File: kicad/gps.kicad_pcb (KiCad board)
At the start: 4 copper layers, 84.1 x 61.7 mm, 68 parts, among them J1 Bus_PCI_Express_x1, J2 USB_C_Receptacle_USB2.0_16P, J3 Conn_01x02, J4 USB_C_Receptacle_USB2.0_16P, Q1 IRLML6344, U2 W25Q128JVP, U3 MCP25625T-E/ML, U4 RP2040, U5 NEO-M9N, X1 ABM8-272-T3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

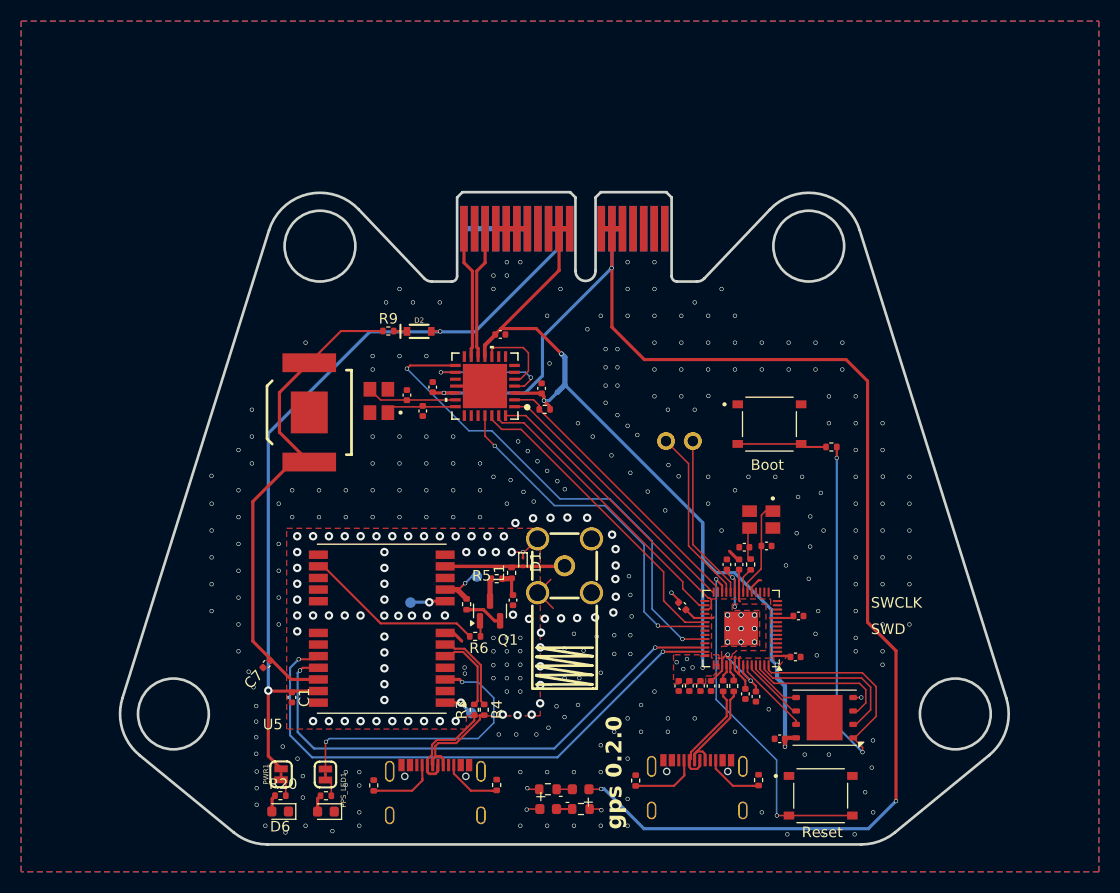
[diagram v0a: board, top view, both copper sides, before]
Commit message: Fix Battery Position
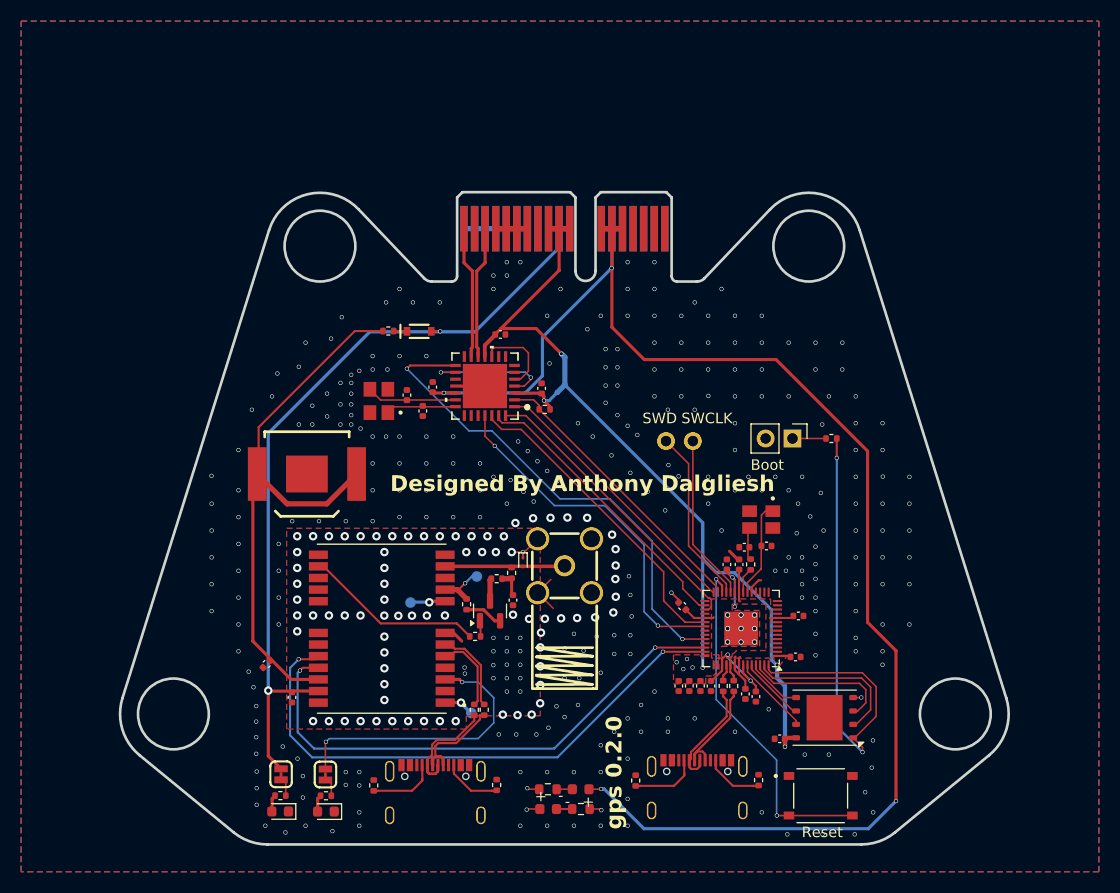
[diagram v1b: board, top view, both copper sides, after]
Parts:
- removed S1: TS-1187A-B-A-B, TS-1187A-B-A-B:SW_TS-1187A-B-A-B
- added J5: Conn_01x02_Pin, Connector_PinHeader_2.54mm:PinHeader_1x02_P2.54mm_Vertical, F.Cu at (168.0, 84.0)
- moved BAT1 5.84 mm to (122.0, 87.4), turned to 0 degrees
- moved R8 0.80 mm to (171.7, 84.0)
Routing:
- net /BACKUP: track 47.8 -> 55.4 mm
- net /~{USB_BOOT_S}: track 8.76 -> 3.18 mm
- net +5V: track 140.9 -> 137.0 mm
- net GND: track 29.0 -> 30.7 mm, vias 357 -> 389
- net /QSPI_SS: track 48.8 -> 49.6 mm
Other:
- board text added: "Designed By Anthony Dalgliesh"

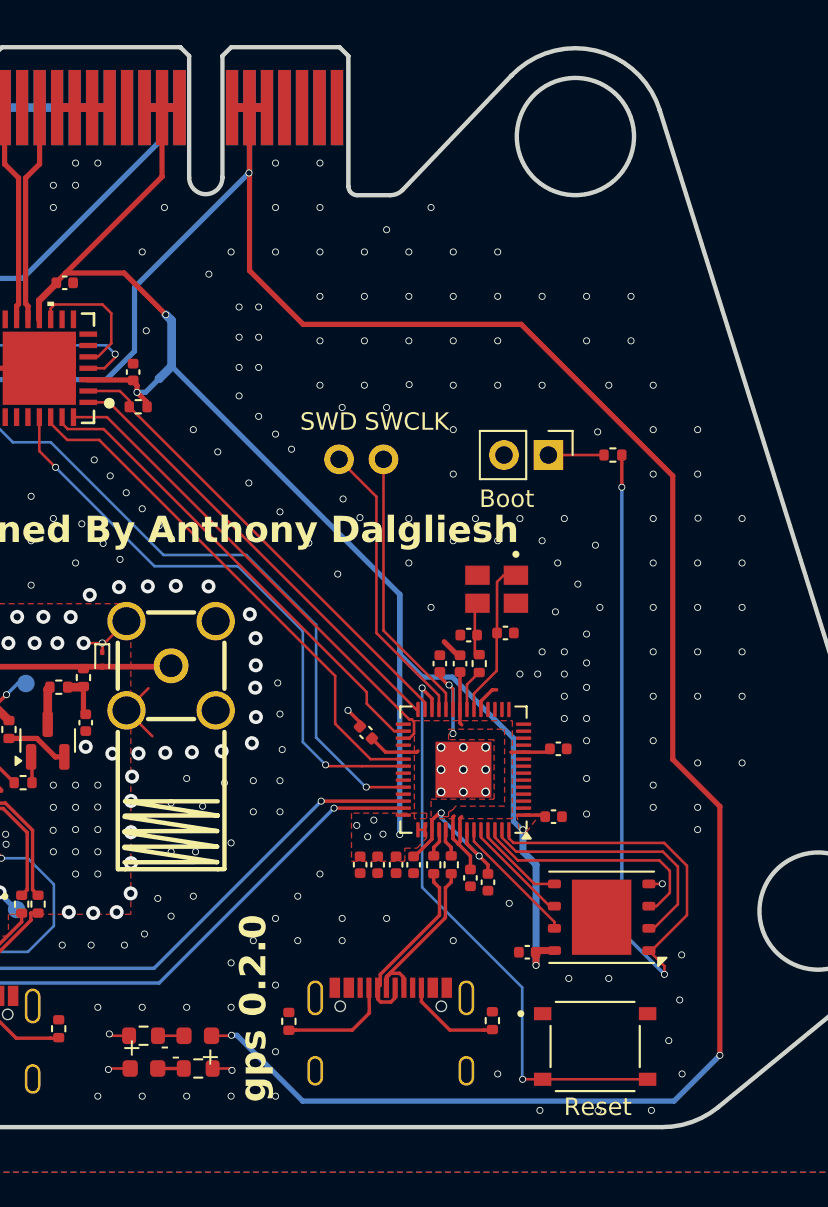
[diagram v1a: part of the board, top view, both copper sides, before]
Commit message: Update components for order
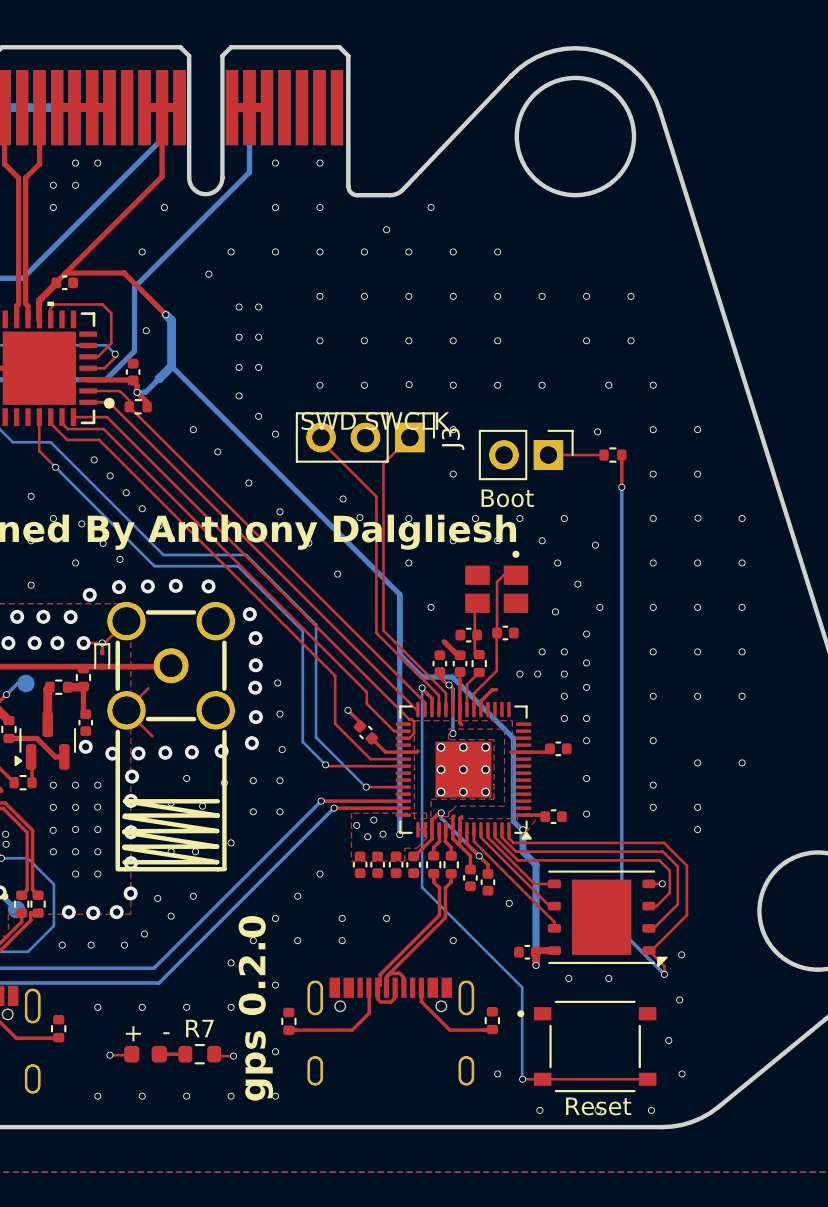
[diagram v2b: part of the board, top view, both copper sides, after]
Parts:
- removed D4: LED, LED_SMD:LED_0603_1608Metric
- removed R10, R13: 1k, Resistor_SMD:R_0603_1608Metric
- added R7: 1 k, Resistor_SMD:R_0603_1608Metric, F.Cu at (148.1, 118.2)
- J3: value Conn_01x02 -> Conn_01x03; footprint Connector_PinHeader_2.54mm:PinHeader_1x02_P2.54mm_Vertical -> Connector_PinHeader_2.54mm:PinHeader_1x03_P2.54mm_Vertical
- moved J3 1.96 mm to (160.1, 83.0)
- moved D3 0.82 mm to (145.0, 118.2)
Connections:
- J3 pad 2: /SWD -> GND
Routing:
- net +5V: track 137.0 -> 32.7 mm, vias 4 -> 1
- net /SWCLK: track 15.8 -> 17.7 mm
- net /SWD: track 16.7 -> 18.3 mm
- net Net-(D4-K): track 1.49 -> 0.00 mm
- net GND: track 30.7 -> 29.5 mm, vias 389 -> 385

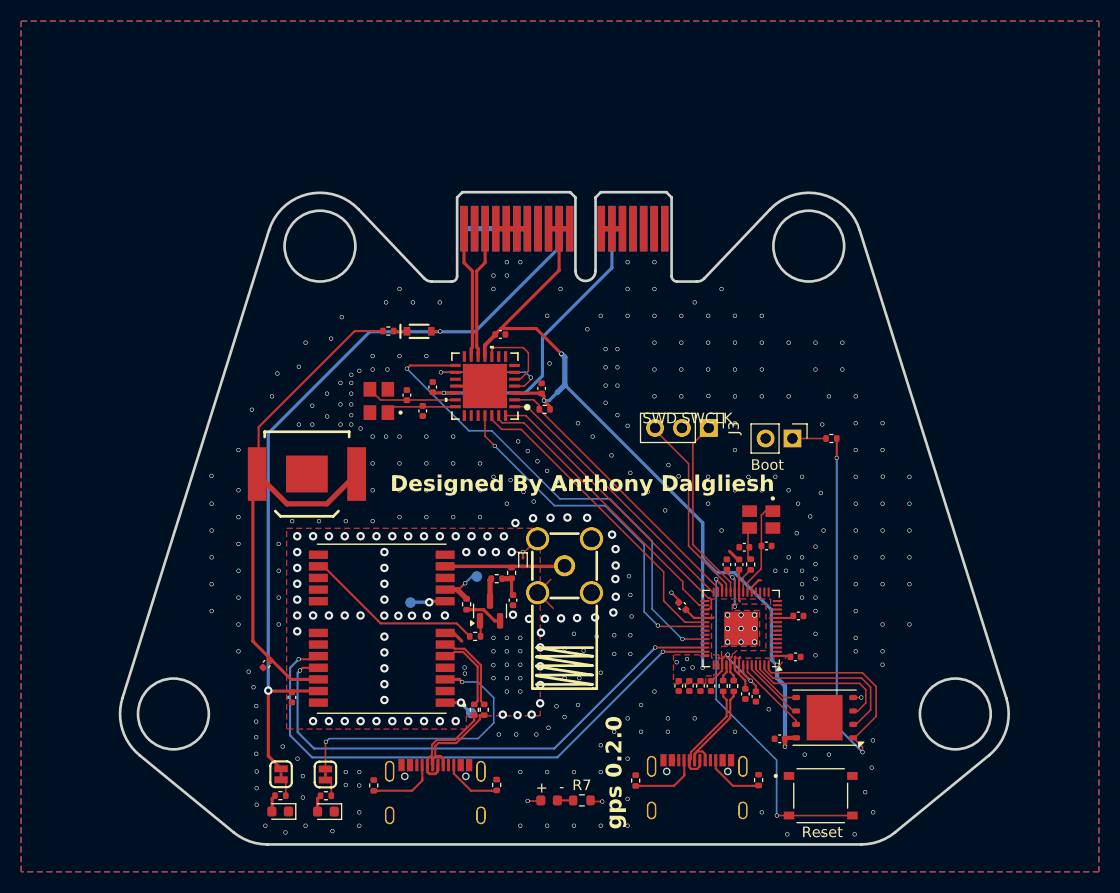
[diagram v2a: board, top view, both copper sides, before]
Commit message: Move Boot pins
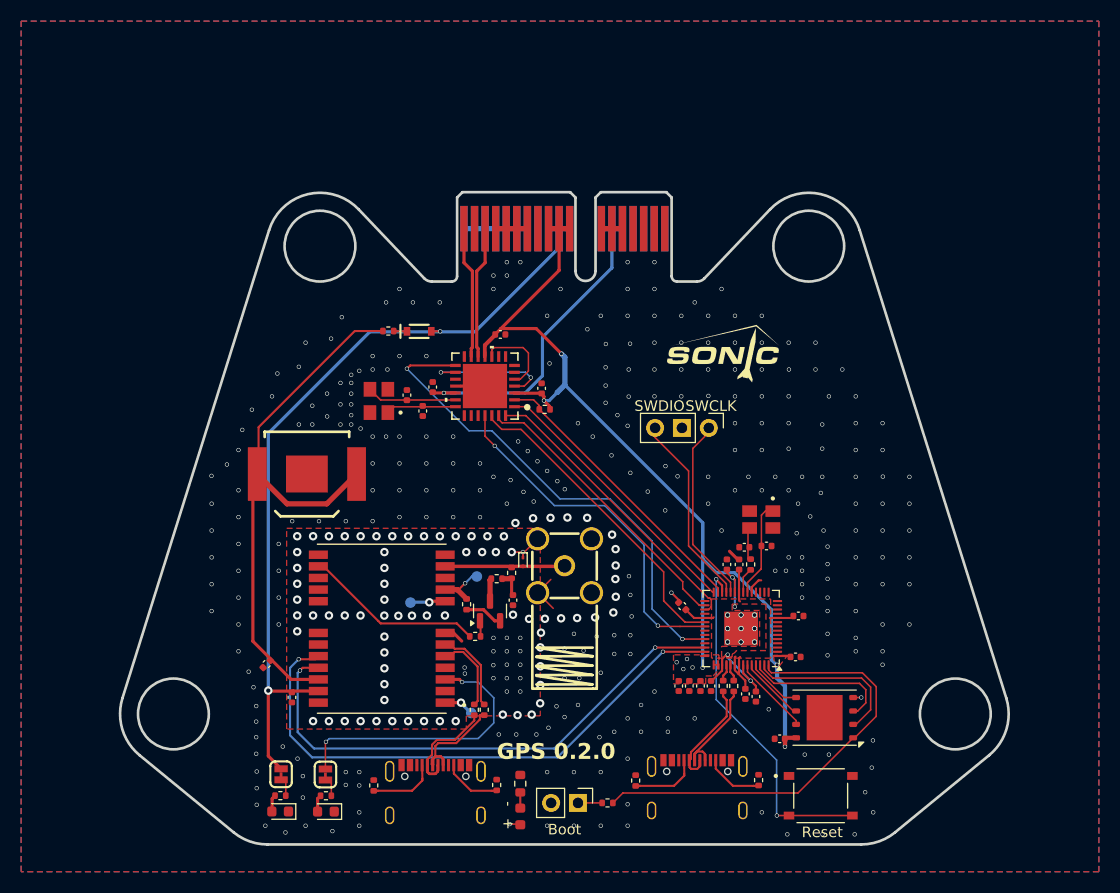
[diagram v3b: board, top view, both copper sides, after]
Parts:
- moved R8 40.5 mm to (150.5, 118.5)
- moved J5 40.0 mm to (147.7, 118.5)
- moved R7 6.04 mm to (142.2, 116.7), turned to 90 degrees
- moved D3 3.12 mm to (142.2, 119.8), turned to -90 degrees
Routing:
- net /QSPI_SS: track 49.6 -> 42.4 mm, vias 2 -> 0
- net GND: track 29.5 -> 28.3 mm, vias 385 -> 390
- net /~{USB_BOOT_S}: track 3.18 -> 2.28 mm
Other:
- board text added: "Anthony D."
- board text added: "GPS 0.2.0"
- board text added: "SWDIO"
- board text removed: "Designed By Anthony Dalgliesh"
- board text removed: "SWD"
- board text removed: "gps 0.2.0"

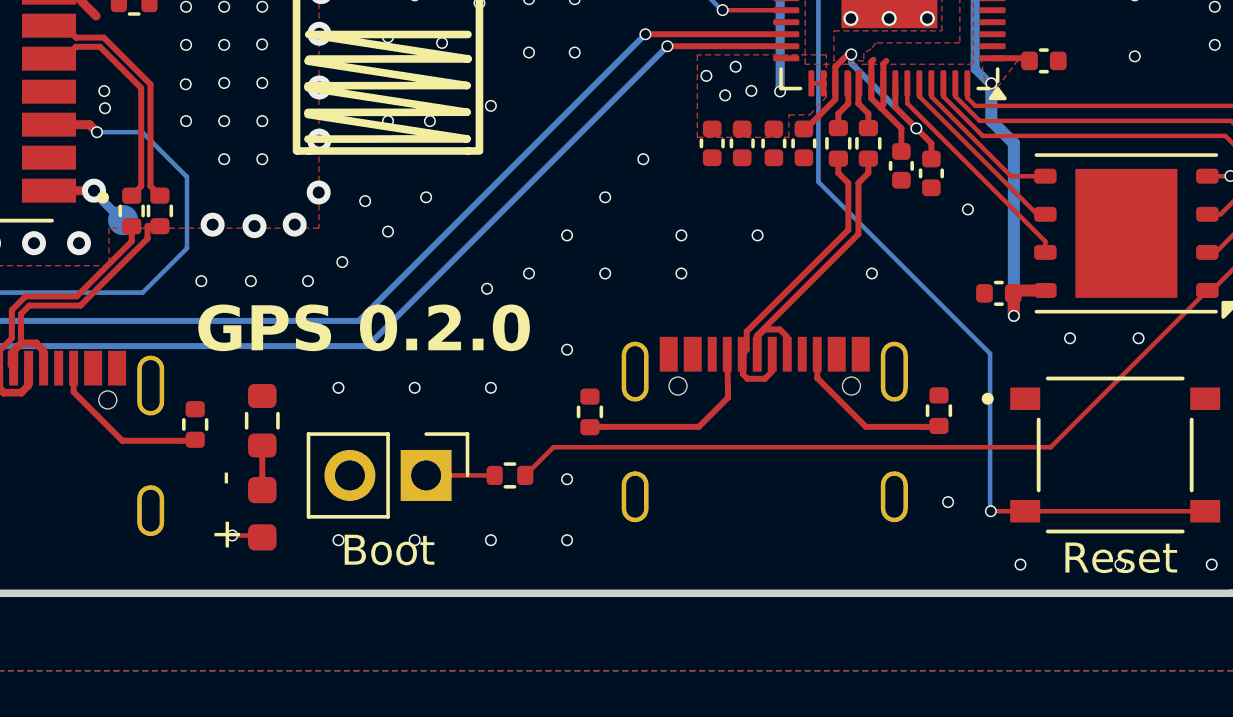
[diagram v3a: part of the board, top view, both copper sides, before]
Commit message: Fix Usb Position
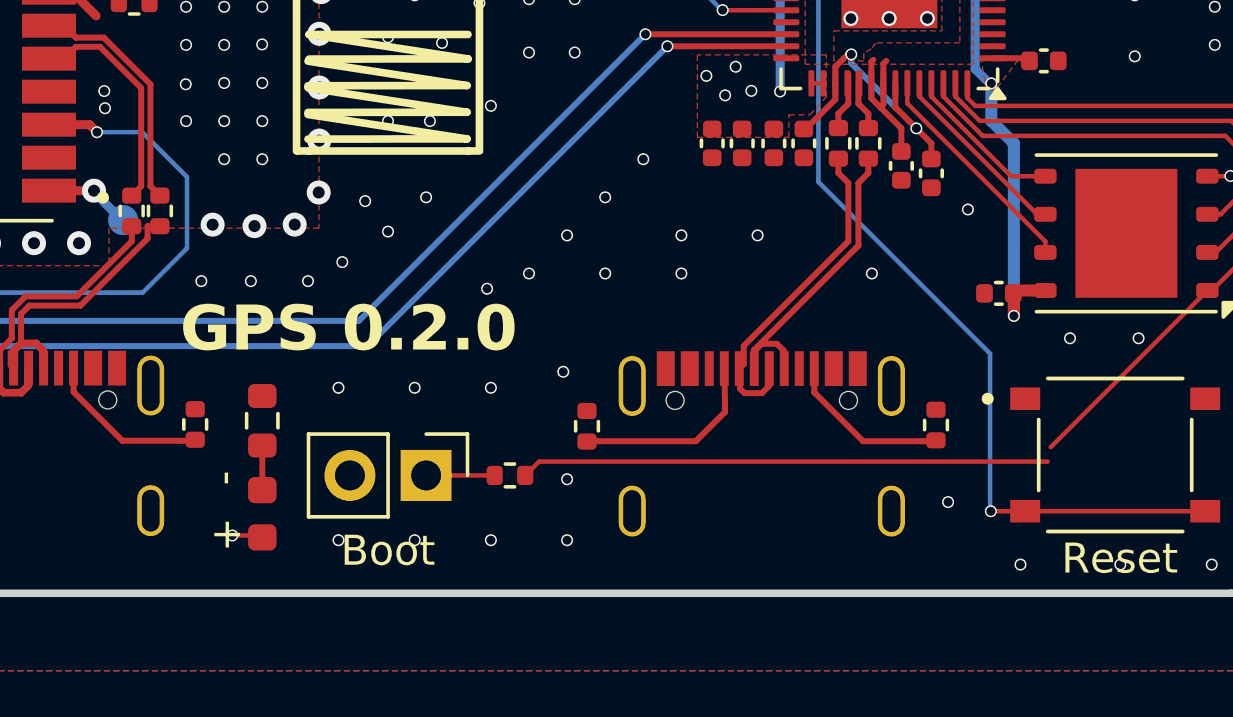
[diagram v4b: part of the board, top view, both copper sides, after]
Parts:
- moved J2 0.49 mm to (158.9, 117.4)
- moved R11 0.49 mm to (153.1, 116.9)
- moved R12 0.49 mm to (164.7, 116.8)
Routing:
- net USB_D+: track 10.4 -> 10.9 mm
- net USB_D-: track 10.5 -> 11.0 mm
